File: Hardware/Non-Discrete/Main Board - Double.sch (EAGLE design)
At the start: 80 parts, among them J1 MICROMOD-2222-C, J10 MICRO-SD-PUSH-PUSH-EXT-PIN, J2 Vertical Qwiic Connector, J4 QWIIC_RIGHT_ANGLE, J5 CORTEX_JTAG_DEBUG_MINIMUM_PTH, J6 MICROMOD_FUNCTION_MAIN, J7 MICROMOD_FUNCTION_MAIN, Q1 3.1A/30V/105mΩ, U1 STG3856QTR, U2 MCP73831, U3 ESD Diode, U4 AP7347DQ-33W5-7K-3.3V, U5 AP7361C-33

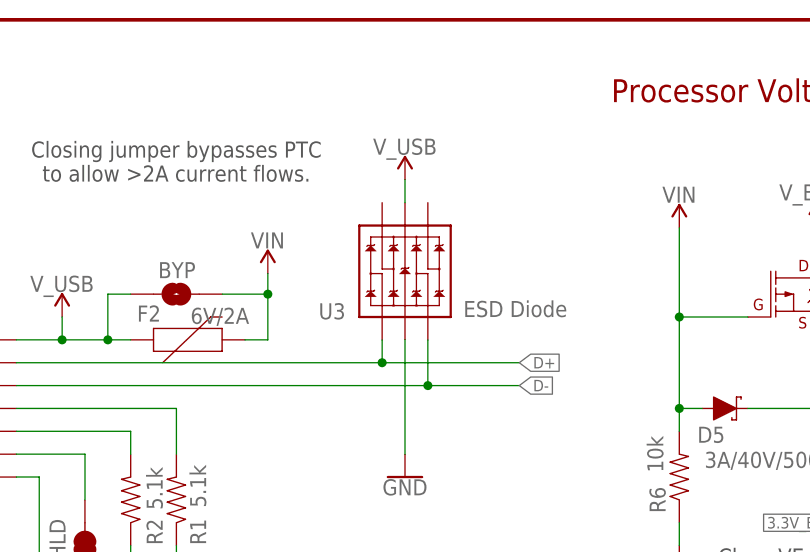
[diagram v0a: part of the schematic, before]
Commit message: Adds ICs necessary for discrete UART switcher to library
* Places new parts into "discrete" version of the main board.
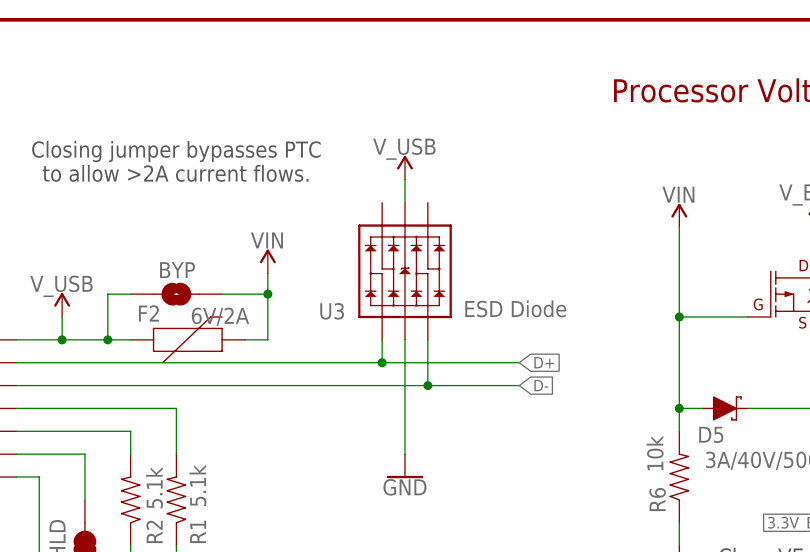
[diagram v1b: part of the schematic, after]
